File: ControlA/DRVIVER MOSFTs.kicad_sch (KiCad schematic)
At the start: 53 parts

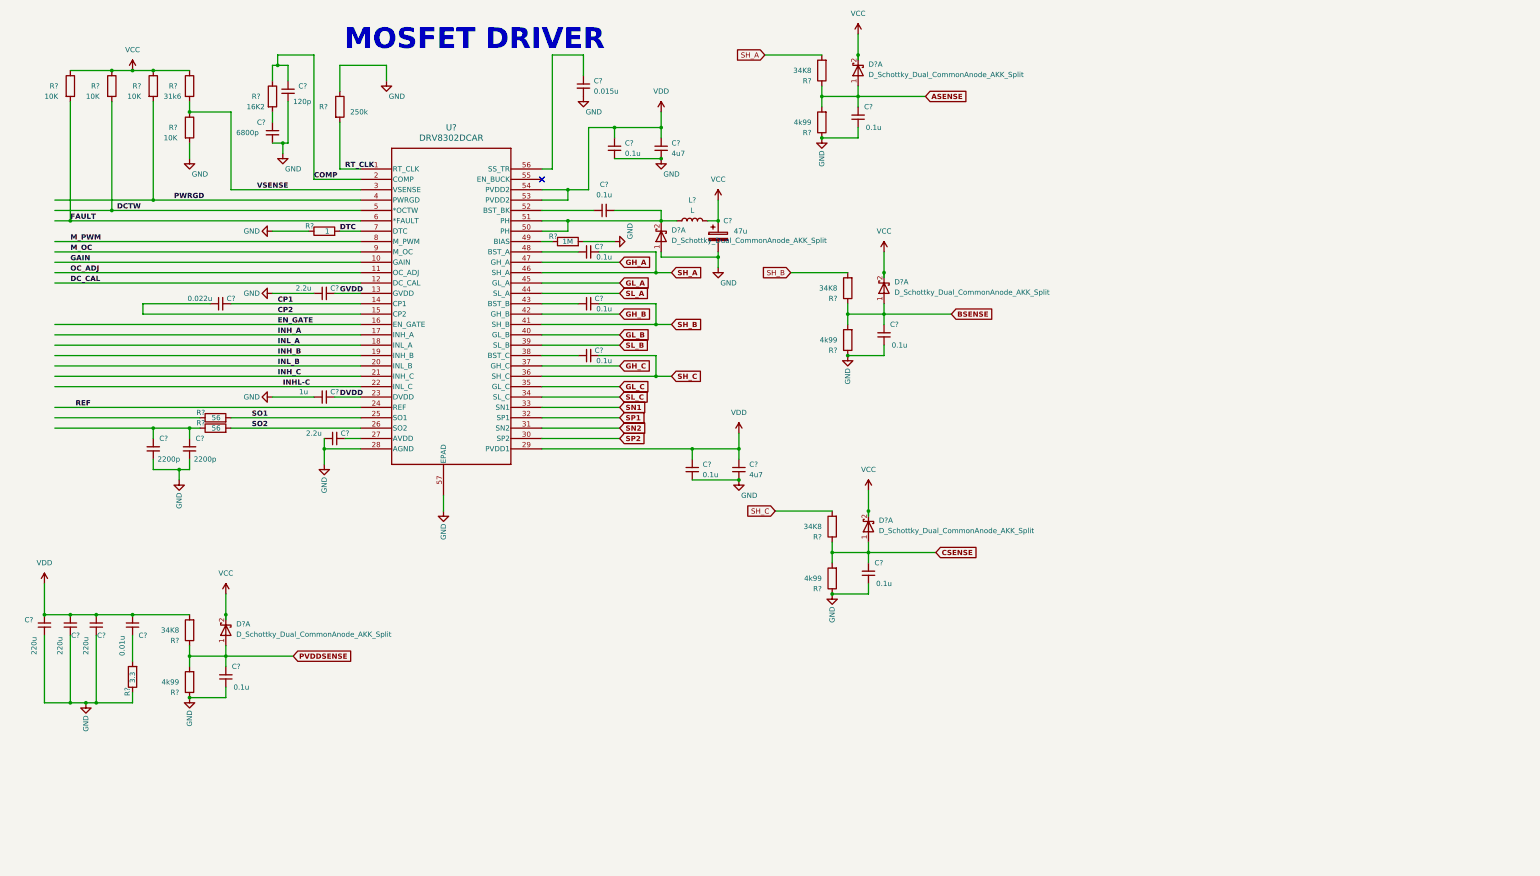
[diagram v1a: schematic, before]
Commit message: final shema symbole
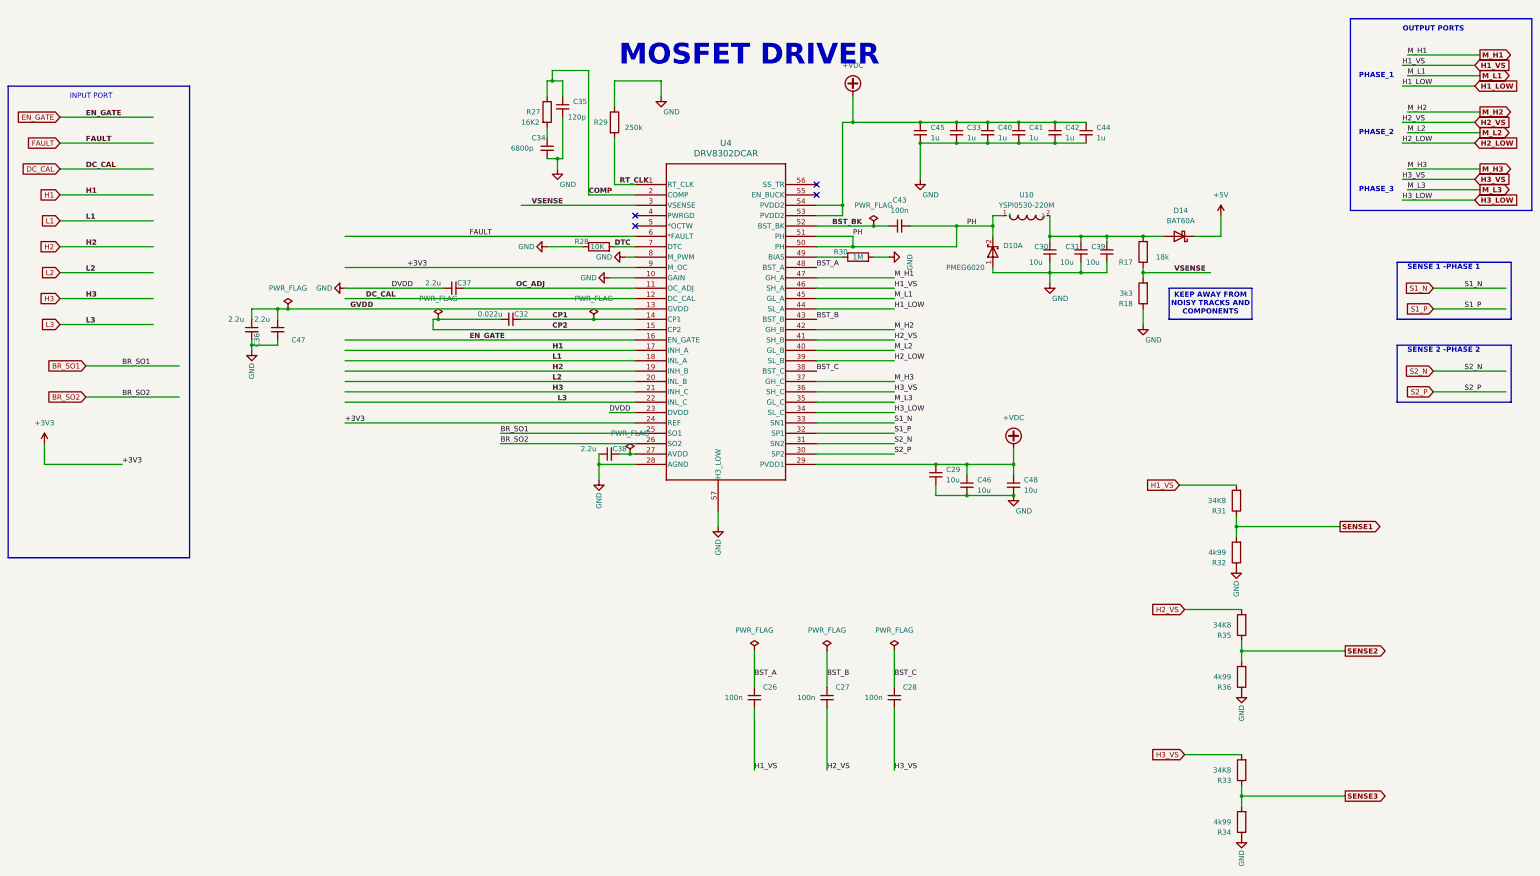
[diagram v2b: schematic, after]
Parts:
- removed C?: 1u, symbol Device:C_Small
- removed C? (x8): 0.1u, symbol Device:C_Small
- removed C? (x2): 2200p, symbol Device:C_Small
- removed C? (x3): 220u, symbol Device:C_Small
- removed C?: 0.01u, symbol Device:C_Small
- removed C?: 47u, symbol Device:C_Polarized
- removed C?: 0.015u, symbol Device:C_Small
- removed D? (x4): D_Schottky_Dual_CommonAnode_AKK_Split, symbol Device:D_Schottky_Dual_CommonAnode_AKK_Split
- removed L?: L, symbol Device:L
- removed R?: 31k6, symbol Device:R
- removed R? (x4): 10K, symbol Device:R
- removed R? (x2): 56, symbol Device:R
- removed R?: 3.3, symbol Device:R
- removed R?: 4k99, symbol Device:R
- removed R?: 34K8, symbol Device:R
- added C26, C27, C28: 100n, Capacitor_SMD:C_0805_2012Metric, symbol Device:C_Small
- added C29, C30, C31, C39: 10u, Capacitor_SMD:C_0805_2012Metric, symbol Device:C_Small
- added C33, C40, C41, C42, C44: 1u, Capacitor_SMD:C_0805_2012Metric, symbol Device:C_Small
- added C37, C47: 2.2u, Capacitor_SMD:C_0805_2012Metric, symbol Device:C_Small
- added D14: BAT60A, Diode_SMD:D_SOD-323, symbol Diode:BAT60A
- added R17: 18k, Resistor_SMD:R_0805_2012Metric, symbol Device:R
- added R18: 3k3, Resistor_SMD:R_0805_2012Metric, symbol Device:R
- added U10: YSPI0530-220M, footprint:IND-SMD_L5.4-W5.2-YSPI0530-220M, symbol YSPI0530-220M:YSPI0530-220M
- C32, C34, C35, C36, C38: renamed from C?; footprint (none) -> Capacitor_SMD:C_0805_2012Metric
- C43: renamed from C?; value 0.1u -> 100n; footprint (none) -> Capacitor_SMD:C_0805_2012Metric
- C45: renamed from C?; value 4u7 -> 1u; footprint (none) -> Capacitor_SMD:C_0805_2012Metric
- C46: renamed from C?; value 0.1u -> 10u; footprint (none) -> Capacitor_SMD:C_0805_2012Metric
- C48: renamed from C?; value 4u7 -> 10u; footprint (none) -> Capacitor_SMD:C_0805_2012Metric
- D10: renamed from D?; value D_Schottky_Dual_CommonAnode_AKK_Split -> PMEG6020; footprint (none) -> footprint:SOD-123_L2.8-W1.8-LS3.7-RD
- R27, R29, R30, R31, R32, R33, R34, R35, R36: renamed from R?; footprint (none) -> Resistor_SMD:R_0805_2012Metric
- R28: renamed from R?; value 1 -> 10K; footprint (none) -> Resistor_SMD:R_0805_2012Metric
- U4: renamed from U?; footprint DCA56_6P35X3P61 -> footprint:DCA56_6P35X3P61-M
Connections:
- net DVDD is gone; now on net GND: U4.23 (DVDD)
- net GAIN is gone; now on net GND: U4.10 (GAIN)
- net M_PWM is gone; now on net GND: U4.8 (M_PWM)
- net REF is gone; now on net +3V3: U4.24 (REF)
- net GND: now also C36.2, C29.2, C30.2, C31.2, C33.2, C37.1, C39.2, C40.2, C41.2, C42.2, C44.2, C47.2, R18.1; no longer C36.1
- net GVDD: now also C36.1, C47.1; no longer C36.2
- net OC_ADJ: now also C37.2
- net VSENSE: now also R17.1, R18.2
- net BST_B: now reaches U4.43 (BST_B)
- net BST_B: now also C27.1
- net BST_C: now reaches U4.38 (BST_C)
- net BST_C: now also C28.1
- net BST_A: now reaches U4.48 (BST_A)
- net BST_A: now also C26.1
- net PH: now reaches C43.2, D10.2 (K), U4.50 (PH), U4.51 (PH)
- net PH: now also U10.1
- net BST_BK: now reaches C43.1, U4.52 (BST_BK)
- net ASENSE renamed SENSE1
- net BSENSE renamed SENSE2
- net CSENSE renamed SENSE3
- net DCTW: no longer names the net of U4.5 (*OCTW)
- net GH_A renamed M_H1
- net GH_B renamed M_H2
- net GH_C renamed M_H3
- net GL_A renamed M_L1
- net GL_B renamed M_L2
- net GL_C renamed M_L3
- net INHL-C renamed L3
- net INH_A renamed H1
- net INH_B renamed H2
- net INH_C renamed H3
- net INL_A renamed L1
- net INL_B renamed L2
- net M_OC renamed +3V3
- net PWRGD: no longer names the net of U4.4 (PWRGD)
- net SH_A renamed H1_VS
- net H1_VS: now also C26.2
- net SH_B renamed H2_VS
- net H2_VS: now also C27.2
- net SH_C renamed H3_VS
- net H3_VS: now also C28.2
- net SL_A renamed H1_LOW
- net SL_B renamed H2_LOW
- net SL_C renamed H3_LOW
- net SN1 renamed S1_N
- net SN2 renamed S2_N
- net SO1 renamed BR_SO1
- net SO2 renamed BR_SO2
- net SP1 renamed S1_P
- net SP2 renamed S2_P
- net VDD renamed +VDC
- net +VDC: now also C29.1, C33.1, C40.1, C41.1, C42.1, C44.1
- new net: C30.1, C31.1, C39.1, D14.2 (A), R17.2, U10.2
- new net +5V: D14.1 (K)
- no-connect marks 1 -> 4
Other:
- note added: "INPUT PORT"
- note added: "KEEP AWAY FROM NOISY TRACKS AND COMPONENTS"
- note added: "OUTPUT PORTS"
- note added: "PHASE_1"
- note added: "PHASE_2"
- note added: "PHASE_3"
- note added: "SENSE 1 -PHASE 1"
- note added: "SENSE 2 -PHASE 2"
- moved on the sheet: C32, C34, C35, C36, C38, C43, C45, C46, C48, D10A, R27, R28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

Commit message: CHANGE V11
change v1
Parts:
- C26, C27, C28, C29, C30, C31, C32, C33, C34, C35, C36, C37, C38, C39, C40, C41, C42, C43, C44, C45, C46, C47, C48: footprint Capacitor_SMD:C_0805_2012Metric -> Capacitor_SMD:C_0603_1608Metric
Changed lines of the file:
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@@
 			)
 		)
-		(property "Footprint" "Capacitor_SMD:C_0805_2012Metric"
+		(property "Footprint" "Capacitor_SMD:C_0603_1608Metric"
 			(at 138.43 82.55 0)
 			(effects
@@
 			)
 		)
-		(property "Footprint" "Capacitor_SMD:C_0805_2012Metric"
+		(property "Footprint" "Capacitor_SMD:C_0603_1608Metric"
 			(at 284.48 73.66 0)
 			(effects
@@
 			)
 		)
-		(property "Footprint" "Capacitor_SMD:C_0805_2012Metric"
+		(property "Footprint" "Capacitor_SMD:C_0603_1608Metric"
 			(at 285.75 44.45 0)
 			(effects
@@
 			)
 		)
-		(property "Footprint" "Capacitor_SMD:C_0805_2012Metric"
+		(property "Footprint" "Capacitor_SMD:C_0603_1608Metric"
 			(at 152.4 90.17 0)
 			(effects
@@
 			)
 		)
-		(property "Footprint" "Capacitor_SMD:C_0805_2012Metric"
+		(property "Footprint" "Capacitor_SMD:C_0603_1608Metric"
 			(at 165.1 38.1 0)
 			(effects
@@
 			)
 		)
-		(property "Footprint" "Capacitor_SMD:C_0805_2012Metric"
+		(property "Footprint" "Capacitor_SMD:C_0603_1608Metric"
 			(at 276.86 44.45 0)
 			(effects
@@
 			)
 		)
-		(property "Footprint" "Capacitor_SMD:C_0805_2012Metric"
+		(property "Footprint" "Capacitor_SMD:C_0603_1608Metric"
 			(at 161.29 48.26 0)
 			(effects
@@
 			)
 		)
-		(property "Footprint" "Capacitor_SMD:C_0805_2012Metric"
+		(property "Footprint" "Capacitor_SMD:C_0603_1608Metric"
 			(at 292.1 73.66 0)
 			(effects
@@
 			)
 		)
-		(property "Footprint" "Capacitor_SMD:C_0805_2012Metric"
+		(property "Footprint" "Capacitor_SMD:C_0603_1608Metric"
 			(at 247.65 67.31 0)
 			(effects
@@
 			)
 		)
-		(property "Footprint" "Capacitor_SMD:C_0805_2012Metric"
+		(property "Footprint" "Capacitor_SMD:C_0603_1608Metric"
 			(at 275.59 130.81 0)
 			(effects
@@
 			)
 		)
-		(property "Footprint" "Capacitor_SMD:C_0805_2012Metric"
+		(property "Footprint" "Capacitor_SMD:C_0603_1608Metric"
 			(at 261.62 44.45 0)
 			(effects
@@
 			)
 		)
-		(property "Footprint" "Capacitor_SMD:C_0805_2012Metric"
+		(property "Footprint" "Capacitor_SMD:C_0603_1608Metric"
 			(at 252.73 44.45 0)
 			(effects
@@
 			)
 		)
-		(property "Footprint" "Capacitor_SMD:C_0805_2012Metric"
+		(property "Footprint" "Capacitor_SMD:C_0603_1608Metric"
 			(at 269.24 44.45 0)
 			(effects
@@
 			)
 		)
-		(property "Footprint" "Capacitor_SMD:C_0805_2012Metric"
+		(property "Footprint" "Capacitor_SMD:C_0603_1608Metric"
 			(at 176.53 123.19 0)
 			(effects
@@
 			)
 		)
-		(property "Footprint" "Capacitor_SMD:C_0805_2012Metric"
+		(property "Footprint" "Capacitor_SMD:C_0603_1608Metric"
 			(at 229.87 182.88 0)
 			(effects
@@
 			)
 		)
-		(property "Footprint" "Capacitor_SMD:C_0805_2012Metric"
+		(property "Footprint" "Capacitor_SMD:C_0603_1608Metric"
 			(at 256.54 128.27 0)
 			(effects
@@
 			)
 		)
-		(property "Footprint" "Capacitor_SMD:C_0805_2012Metric"
+		(property "Footprint" "Capacitor_SMD:C_0603_1608Metric"
 			(at 264.16 130.81 0)
 			(effects
@@
 			)
 		)
-		(property "Footprint" "Capacitor_SMD:C_0805_2012Metric"
+		(property "Footprint" "Capacitor_SMD:C_0603_1608Metric"
 			(at 293.37 44.45 0)
 			(effects
@@
 			)
 		)
-		(property "Footprint" "Capacitor_SMD:C_0805_2012Metric"
+		(property "Footprint" "Capacitor_SMD:C_0603_1608Metric"
 			(at 246.38 182.88 0)
 			(effects
@@
 			)
 		)
-		(property "Footprint" "Capacitor_SMD:C_0805_2012Metric"
+		(property "Footprint" "Capacitor_SMD:C_0603_1608Metric"
 			(at 212.09 182.88 0)
 			(effects
@@
 			)
 		)
-		(property "Footprint" "Capacitor_SMD:C_0805_2012Metric"
+		(property "Footprint" "Capacitor_SMD:C_0603_1608Metric"
 			(at 95.25 92.71 0)
 			(effects
@@
 			)
 		)
-		(property "Footprint" "Capacitor_SMD:C_0805_2012Metric"
+		(property "Footprint" "Capacitor_SMD:C_0603_1608Metric"
 			(at 88.9 92.71 0)
 			(effects
@@
 			)
 		)
-		(property "Footprint" "Capacitor_SMD:C_0805_2012Metric"
+		(property "Footprint" "Capacitor_SMD:C_0603_1608Metric"
 			(at 298.45 73.66 0)
 			(effects
